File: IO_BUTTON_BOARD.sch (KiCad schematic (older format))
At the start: 118 parts

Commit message: Add reverse current protection, generate netlist, add footprints
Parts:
- added D2: D, Diodes_SMD:D_0805, symbol D
- C1: renamed from C?; footprint (none) -> Capacitors_SMD:c_elec_4x4.5
- D1, D10, D11, D12, D13, D14, D15, D16, D17, D18, D19, D3, D4, D5, D6, D7, D8, D9: renamed from D?; footprint (none) -> LEDs:LED_0805
- P1: renamed from P?; value I2C3 -> I2C; footprint (none) -> Pin_Headers:Pin_Header_Straight_1x04
- P10: renamed from P?; value IO_0 -> IO_7; footprint (none) -> Pin_Headers:Pin_Header_Straight_1x04
- P2, P3: renamed from P?; footprint (none) -> Pin_Headers:Pin_Header_Straight_1x04
- P4: renamed from P?; value IO_0 -> IO_1; footprint (none) -> Pin_Headers:Pin_Header_Straight_1x04
- P5: renamed from P?; value IO_0 -> IO_2; footprint (none) -> Pin_Headers:Pin_Header_Straight_1x04
- P6: renamed from P?; value IO_0 -> IO_3; footprint (none) -> Pin_Headers:Pin_Header_Straight_1x04
- P7: renamed from P?; value IO_0 -> IO_4; footprint (none) -> Pin_Headers:Pin_Header_Straight_1x04
- P8: renamed from P?; value IO_0 -> IO_5; footprint (none) -> Pin_Headers:Pin_Header_Straight_1x04
- P9: renamed from P?; value IO_0 -> IO_6; footprint (none) -> Pin_Headers:Pin_Header_Straight_1x04
- Q1, Q10, Q11, Q12, Q2, Q3, Q4, Q5, Q6, Q7, Q8, Q9: renamed from Q?; footprint (none) -> TO_SOT_Packages_SMD:SOT-23
- Q13: renamed from Q?; footprint (none) -> Resistors_SMD:R_0805
- R1, R10, R11, R12, R13, R14, R15, R16, R17, R18, R19, R2, R20, R21, R22, R23, R24, R25, R26, R27, R28, R29, R3, R30, R31, R32, R33, R34, R35, R36, R37, R38, R39, R4, R40, R41, R42, R43, R44, R45, R46, R47, R48, R49, R5, R50, R6, R7, R8, R9: renamed from R?; footprint (none) -> Resistors_SMD:R_0805
- S1, S2, S3, S4, S5, S6, S7, S8: renamed from S?; footprint (none) -> Pin_Headers:Pin_Header_Straight_1x03
- SW1: renamed from SW?; footprint (none) -> Housings_DIP:DIP-8_W7.62mm
- SW2, SW3, SW4, SW5, SW6, SW7, SW8, SW9: renamed from SW?; footprint (none) -> Buttons_Switches_SMD:SW_SPST_EVQPE1
- U1: renamed from U?; footprint (none) -> Housings_SOIC:SOIC-16W_7.5x10.3mm_Pitch1.27mm
- U2, U3: renamed from U?; footprint (none) -> SMD_Packages:SOIC-14_N
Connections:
- net +5V: now also D2.1 (K); no longer P1.3 (P3), P2.3 (P3)
- new net: D2.2 (A), P1.3 (P3), P2.3 (P3)
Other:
- moved on the sheet: C1, D3, P1, P2, R7

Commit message: Add pcb
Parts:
- Q13: footprint Resistors_SMD:R_0805 -> TO_SOT_Packages_SMD:SOT-23
- S1: value Switch2RT -> IN_0
- S2: value Switch2RT -> IN_1
- S3: value Switch2RT -> IN_2
- S4: value Switch2RT -> IN_3
- S5: value Switch2RT -> IN_4
- S6: value Switch2RT -> IN_5
- S7: value Switch2RT -> IN_6
- S8: value Switch2RT -> IN_7
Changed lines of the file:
@@
 F 0 "Q13" H 9700 10600 50  0000 L CNN
 F 1 "PNP" H 9700 10500 50  0000 L CNN
-F 2 "Resistors_SMD:R_0805" H 9700 10650 50  0001 C CNN
+F 2 "TO_SOT_Packages_SMD:SOT-23" H 9700 10650 50  0001 C CNN
 F 3 "" H 9500 10550 50  0000 C CNN
 	1    9500 10550
@@
 P 11000 700
 F 0 "S1" H 11000 450 60  0000 C CNN
-F 1 "Switch2RT" H 11000 950 60  0000 C CNN
+F 1 "IN_0" H 11000 950 60  0000 C CNN
 F 2 "Pin_Headers:Pin_Header_Straight_1x03" H 10700 750 60  0001 C CNN
 F 3 "" H 10700 750 60  0001 C CNN
@@
 P 11000 1150
 F 0 "S2" H 11000 900 60  0000 C CNN
-F 1 "Switch2RT" H 11000 1400 60  0000 C CNN
+F 1 "IN_1" H 11000 1400 60  0000 C CNN
 F 2 "Pin_Headers:Pin_Header_Straight_1x03" H 10700 1200 60  0001 C CNN
 F 3 "" H 10700 1200 60  0001 C CNN
@@
 P 11000 1600
 F 0 "S3" H 11000 1350 60  0000 C CNN
-F 1 "Switch2RT" H 11000 1850 60  0000 C CNN
+F 1 "IN_2" H 11000 1850 60  0000 C CNN
 F 2 "Pin_Headers:Pin_Header_Straight_1x03" H 10700 1650 60  0001 C CNN
 F 3 "" H 10700 1650 60  0001 C CNN
@@
 P 11000 2050
 F 0 "S4" H 11000 1800 60  0000 C CNN
-F 1 "Switch2RT" H 11000 2300 60  0000 C CNN
+F 1 "IN_3" H 11000 2300 60  0000 C CNN
 F 2 "Pin_Headers:Pin_Header_Straight_1x03" H 10700 2100 60  0001 C CNN
 F 3 "" H 10700 2100 60  0001 C CNN
@@
 P 11000 2650
 F 0 "S5" H 11000 2400 60  0000 C CNN
-F 1 "Switch2RT" H 11000 2900 60  0000 C CNN
+F 1 "IN_4" H 11000 2900 60  0000 C CNN
 F 2 "Pin_Headers:Pin_Header_Straight_1x03" H 10700 2700 60  0001 C CNN
 F 3 "" H 10700 2700 60  0001 C CNN
@@
 P 11000 3100
 F 0 "S6" H 11000 2850 60  0000 C CNN
-F 1 "Switch2RT" H 11000 3350 60  0000 C CNN
+F 1 "IN_5" H 11000 3350 60  0000 C CNN
 F 2 "Pin_Headers:Pin_Header_Straight_1x03" H 10700 3150 60  0001 C CNN
 F 3 "" H 10700 3150 60  0001 C CNN
@@
 P 11000 3550
 F 0 "S7" H 11000 3300 60  0000 C CNN
-F 1 "Switch2RT" H 11000 3800 60  0000 C CNN
+F 1 "IN_6" H 11000 3800 60  0000 C CNN
 F 2 "Pin_Headers:Pin_Header_Straight_1x03" H 10700 3600 60  0001 C CNN
 F 3 "" H 10700 3600 60  0001 C CNN
@@
 P 11000 4000
 F 0 "S8" H 11000 3750 60  0000 C CNN
-F 1 "Switch2RT" H 11000 4250 60  0000 C CNN
+F 1 "IN_7" H 11000 4250 60  0000 C CNN
 F 2 "Pin_Headers:Pin_Header_Straight_1x03" H 10700 4050 60  0001 C CNN
 F 3 "" H 10700 4050 60  0001 C CNN

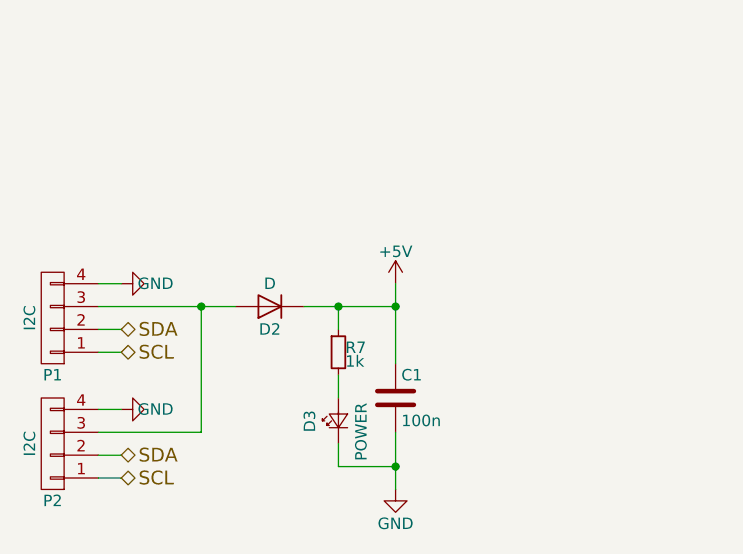
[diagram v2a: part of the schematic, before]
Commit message: Fix VCC disconnected issue Rerouted with larger width
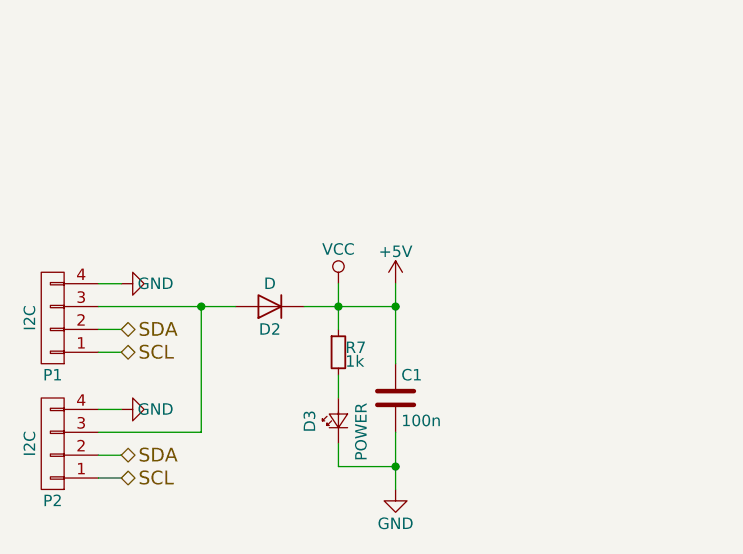
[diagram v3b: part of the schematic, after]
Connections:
- net VCC is gone; now on net +5V: U2.14 (VCC), U2.14 (VCC), U2.14 (VCC), U2.14 (VCC), U3.14 (VCC), U3.14 (VCC), U3.14 (VCC), U3.14 (VCC)
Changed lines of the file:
@@
 	1900 10600 1900 10500
 Wire Wire Line
-	1900 10300 1900 10200
+	1900 10100 1900 10300
 Wire Wire Line
 	1750 10200 2150 10200
@@
 Connection ~ 1900 10200
 Connection ~ 1300 10200
+$Comp
+L VCC #PWR?
+U 1 1 5C767C53
+P 1900 10100
+F 0 "#PWR?" H 1900 9950 50  0001 C CNN
+F 1 "VCC" H 1900 10250 50  0000 C CNN
+F 2 "" H 1900 10100 50  0000 C CNN
+F 3 "" H 1900 10100 50  0000 C CNN
+	1    1900 10100
+	1    0    0    -1
+$EndComp
 $EndSCHEMATC

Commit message: Reroute PCB with 'fake' +5V and GND netlist in order to get different width for PCB tracks
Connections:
- net +5V renamed VCC
- net OUT_0 renamed D_OUT_0
- net OUT_1 renamed D_OUT_1
- net OUT_2 renamed D_OUT_2
- net OUT_3 renamed D_OUT_3
- net OUT_4 renamed D_OUT_4
- net OUT_5 renamed D_OUT_5
- net OUT_6 renamed D_OUT_6
- net OUT_7 renamed D_OUT_7
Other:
- moved on the sheet: C1, D2, D3, P1, P2, R7

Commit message: Change positions and orientation of connectors on the pcb
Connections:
- net D_OUT_0: now also P3.3 (P3); no longer P3.2 (P2)
- net D_OUT_1: now also P4.3 (P3); no longer P4.2 (P2)
- net D_OUT_2: now also P5.3 (P3); no longer P5.2 (P2)
- net D_OUT_3: now also P6.3 (P3); no longer P6.2 (P2)
- net D_OUT_4: now also P7.3 (P3); no longer P7.2 (P2)
- net D_OUT_5: now also P8.3 (P3); no longer P8.2 (P2)
- net D_OUT_6: now also P9.3 (P3); no longer P9.2 (P2)
- net D_OUT_7: now also P10.3 (P3); no longer P10.2 (P2)
- net GND: now also P1.1 (P1), P10.1 (P1), P2.1 (P1), P3.1 (P1), P4.1 (P1), P5.1 (P1), P6.1 (P1), P7.1 (P1), P8.1 (P1), P9.1 (P1); no longer P1.4 (P4), P10.4 (P4), P2.4 (P4), P3.4 (P4), P4.4 (P4), P5.4 (P4), P6.4 (P4), P7.4 (P4), P8.4 (P4), P9.4 (P4)
- net IN_0: now also P3.2 (P2); no longer P3.3 (P3)
- net IN_1: now also P4.2 (P2); no longer P4.3 (P3)
- net IN_2: now also P5.2 (P2); no longer P5.3 (P3)
- net IN_3: now also P6.2 (P2); no longer P6.3 (P3)
- net IN_4: now also P7.2 (P2); no longer P7.3 (P3)
- net IN_5: now also P8.2 (P2); no longer P8.3 (P3)
- net IN_6: now also P9.2 (P2); no longer P9.3 (P3)
- net IN_7: now also P10.2 (P2); no longer P10.3 (P3)
- net SCL: now also P1.3 (P3), P2.3 (P3); no longer P1.1 (P1), P2.1 (P1)
- net SDA: now also P1.4 (P4), P2.4 (P4); no longer P1.2 (P2), P2.2 (P2)
- net VCC: now also P10.4 (P4), P3.4 (P4), P4.4 (P4), P5.4 (P4), P6.4 (P4), P7.4 (P4), P8.4 (P4), P9.4 (P4); no longer P10.1 (P1), P3.1 (P1), P4.1 (P1), P5.1 (P1), P6.1 (P1), P7.1 (P1), P8.1 (P1), P9.1 (P1)
- new net: D2.2 (A), P1.2 (P2), P2.2 (P2)
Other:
- moved on the sheet: P1, P2
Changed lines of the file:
@@
 L CONN_01X04 P2
 U 1 1 5C4ADA31
-P 650 9850
-F 0 "P2" H 650 10100 50  0000 C CNN
-F 1 "I2C" V 750 9850 50  0000 C CNN
-F 2 "Pin_Headers:Pin_Header_Straight_1x04" H 650 9850 50  0001 C CNN
-F 3 "" H 650 9850 50  0000 C CNN
-	1    650  9850
+P 650 9750
+F 0 "P2" H 650 10000 50  0000 C CNN
+F 1 "I2C" V 750 9750 50  0000 C CNN
+F 2 "Pin_Headers:Pin_Header_Straight_1x04" H 650 9750 50  0001 C CNN
+F 3 "" H 650 9750 50  0000 C CNN
+	1    650  9750
 	-1   0    0    1
 $EndComp
-Text HLabel 950  9900 2    60   BiDi ~ 0
+Text HLabel 950  9600 2    60   BiDi ~ 0
 SDA
-Text HLabel 950  10000 2    60   BiDi ~ 0
+Text HLabel 950  9700 2    60   BiDi ~ 0
 SCL
 Text HLabel 3700 4700 0    60   BiDi ~ 0
@@
 L CONN_01X04 P1
 U 1 1 5C4ADDFA
-P 650 9300
-F 0 "P1" H 650 9550 50  0000 C CNN
-F 1 "I2C" V 750 9300 50  0000 C CNN
-F 2 "Pin_Headers:Pin_Header_Straight_1x04" H 650 9300 50  0001 C CNN
-F 3 "" H 650 9300 50  0000 C CNN
-	1    650  9300
+P 650 9200
+F 0 "P1" H 650 9450 50  0000 C CNN
+F 1 "I2C" V 750 9200 50  0000 C CNN
+F 2 "Pin_Headers:Pin_Header_Straight_1x04" H 650 9200 50  0001 C CNN
+F 3 "" H 650 9200 50  0000 C CNN
+	1    650  9200
 	-1   0    0    1
 $EndComp
-Text HLabel 950  9350 2    60   BiDi ~ 0
+Text HLabel 950  9050 2    60   BiDi ~ 0
 SDA
-Text HLabel 950  9450 2    60   BiDi ~ 0
+Text HLabel 950  9150 2    60   BiDi ~ 0
 SCL
 $Comp
@@
 F 3 "" H 15900 900 50  0000 C CNN
 	1    15900 900
-	1    0    0    -1
+	1    0    0    1
 $EndComp
 $Comp
@@
 F 3 "" H 15900 1650 50  0000 C CNN
 	1    15900 1650
-	1    0    0    -1
+	1    0    0    1
 $EndComp
 $Comp
@@
 F 3 "" H 15900 2400 50  0000 C CNN
 	1    15900 2400
-	1    0    0    -1
+	1    0    0    1
 $EndComp
 $Comp
@@
 F 3 "" H 15900 3150 50  0000 C CNN
 	1    15900 3150
-	1    0    0    -1
+	1    0    0    1
 $EndComp
 $Comp
@@
 F 3 "" H 15900 3900 50  0000 C CNN
 	1    15900 3900
-	1    0    0    -1
+	1    0    0    1
 $EndComp
 $Comp
@@
 F 3 "" H 15900 4650 50  0000 C CNN
 	1    15900 4650
-	1    0    0    -1
+	1    0    0    1
 $EndComp
 $Comp
@@
 F 3 "" H 15900 5400 50  0000 C CNN
 	1    15900 5400
-	1    0    0    -1
+	1    0    0    1
 $EndComp
 $Comp
@@
 F 3 "" H 15900 6150 50  0000 C CNN
 	1    15900 6150
-	1    0    0    -1
+	1    0    0    1
 $EndComp
 $Comp
@@
 Connection ~ 2350 5100
 Wire Wire Line
+	850  9900 950  9900
+Wire Wire Line
+	1500 9800 850  9800
+Wire Wire Line
+	3700 4700 3800 4700
+Wire Wire Line
+	3800 4800 3700 4800
+Wire Wire Line
+	850  9600 950  9600
+Wire Wire Line
 	850  9700 950  9700
 Wire Wire Line
-	1500 9800 850  9800
-Wire Wire Line
-	3700 4700 3800 4700
-Wire Wire Line
-	3800 4800 3700 4800
-Wire Wire Line
-	850  9900 950  9900
-Wire Wire Line
-	850  10000 950  10000
+	850  9350 950  9350
+Wire Wire Line
+	850  9250 1650 9250
+Wire Wire Line
+	850  9050 950  9050
 Wire Wire Line
 	850  9150 950  9150
-Wire Wire Line
-	850  9250 1650 9250
-Wire Wire Line
-	850  9350 950  9350
-Wire Wire Line
-	850  9450 950  9450
 Wire Wire Line
 	2800 9650 2800 9550
@@
 Text HLabel 2050 10050 3    60   Input ~ 0
 GND_PWR
-Text HLabel 950  9700 2    60   Input ~ 0
+Text HLabel 950  9900 2    60   Input ~ 0
 GND_PWR
-Text HLabel 950  9150 2    60   Input ~ 0
+Text HLabel 950  9350 2    60   Input ~ 0
 GND_PWR
 Wire Wire Line

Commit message: Fix missing pull resistor Reroute PCB
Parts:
- added R51, R52, R53, R54, R55, R56, R57, R58: 1k, Resistors_SMD:R_0805, symbol R_Small
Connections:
- net IN_0: now also R51.1
- net IN_1: now also R52.1
- net IN_2: now also R53.1
- net IN_3: now also R54.1
- net IN_4: now also R55.1
- net IN_5: now also R56.1
- net IN_6: now also R57.1
- net IN_7: now also R58.1
- net PULL_LANE: now also R51.2, R52.2, R53.2, R54.2, R55.2, R56.2, R57.2, R58.2
- net D_OUT_0 renamed OUT_0
- net D_OUT_1 renamed OUT_1
- net D_OUT_2 renamed OUT_2
- net D_OUT_3 renamed OUT_3
- net D_OUT_4 renamed OUT_4
- net D_OUT_5 renamed OUT_5
- net D_OUT_6 renamed OUT_6
- net D_OUT_7 renamed OUT_7
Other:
- moved on the sheet: D3, R7

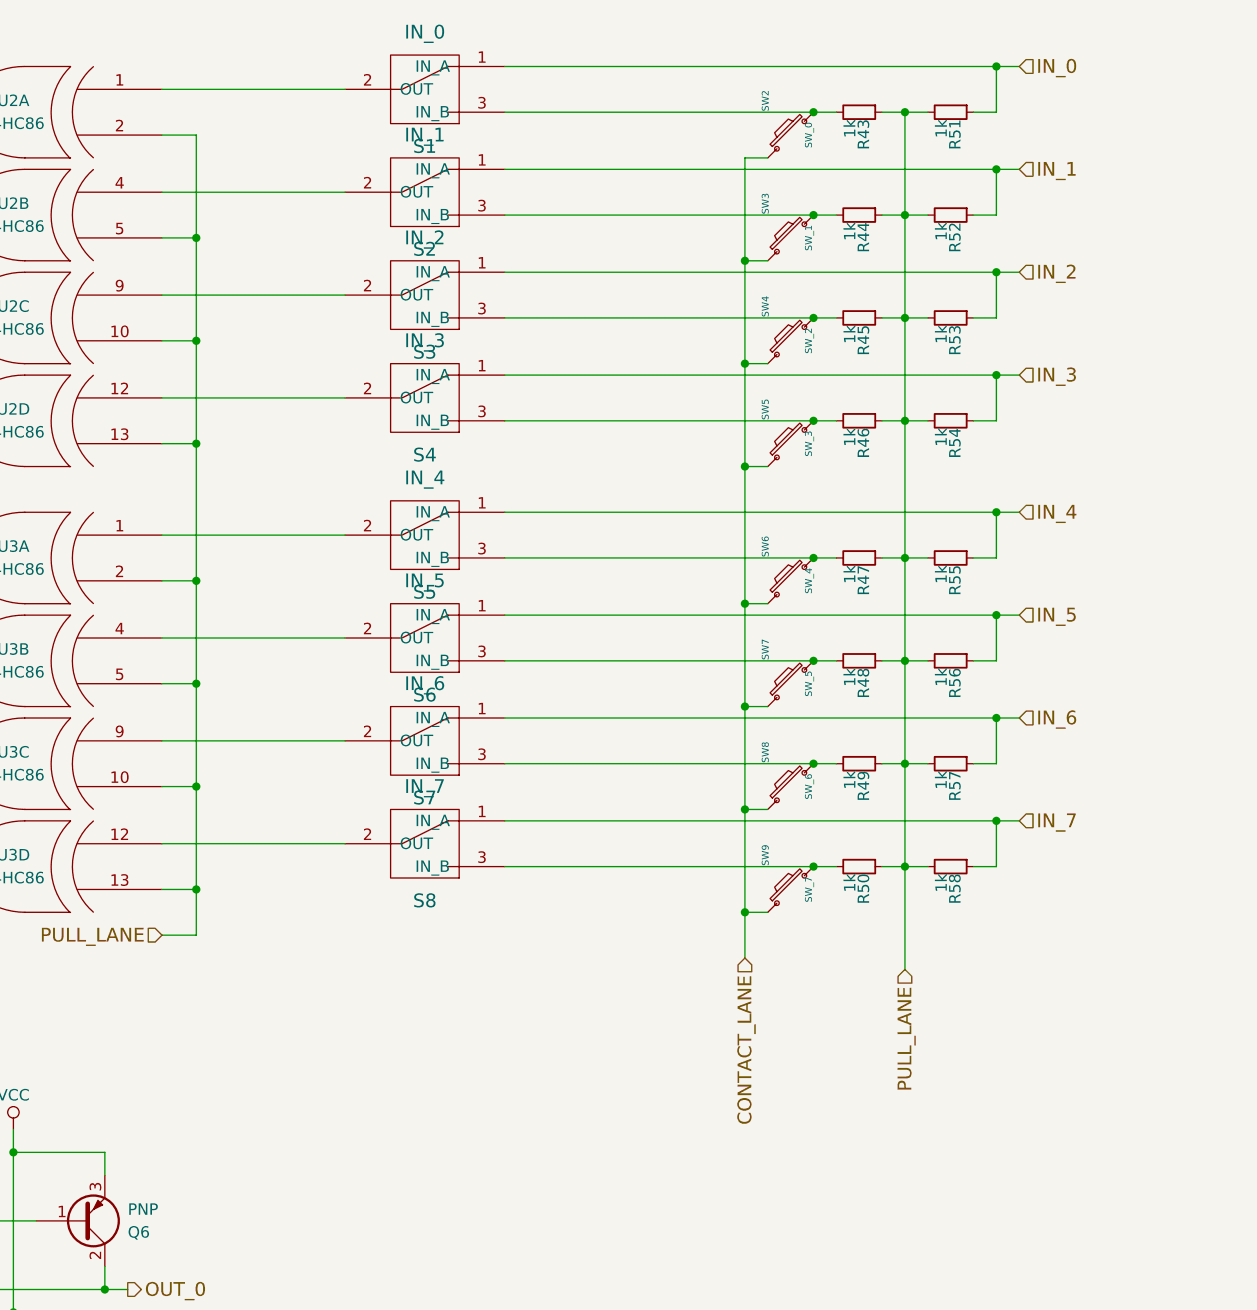
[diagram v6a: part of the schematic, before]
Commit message: Remove useless resistors Todo : develop a system to free XOR outputs on input mode
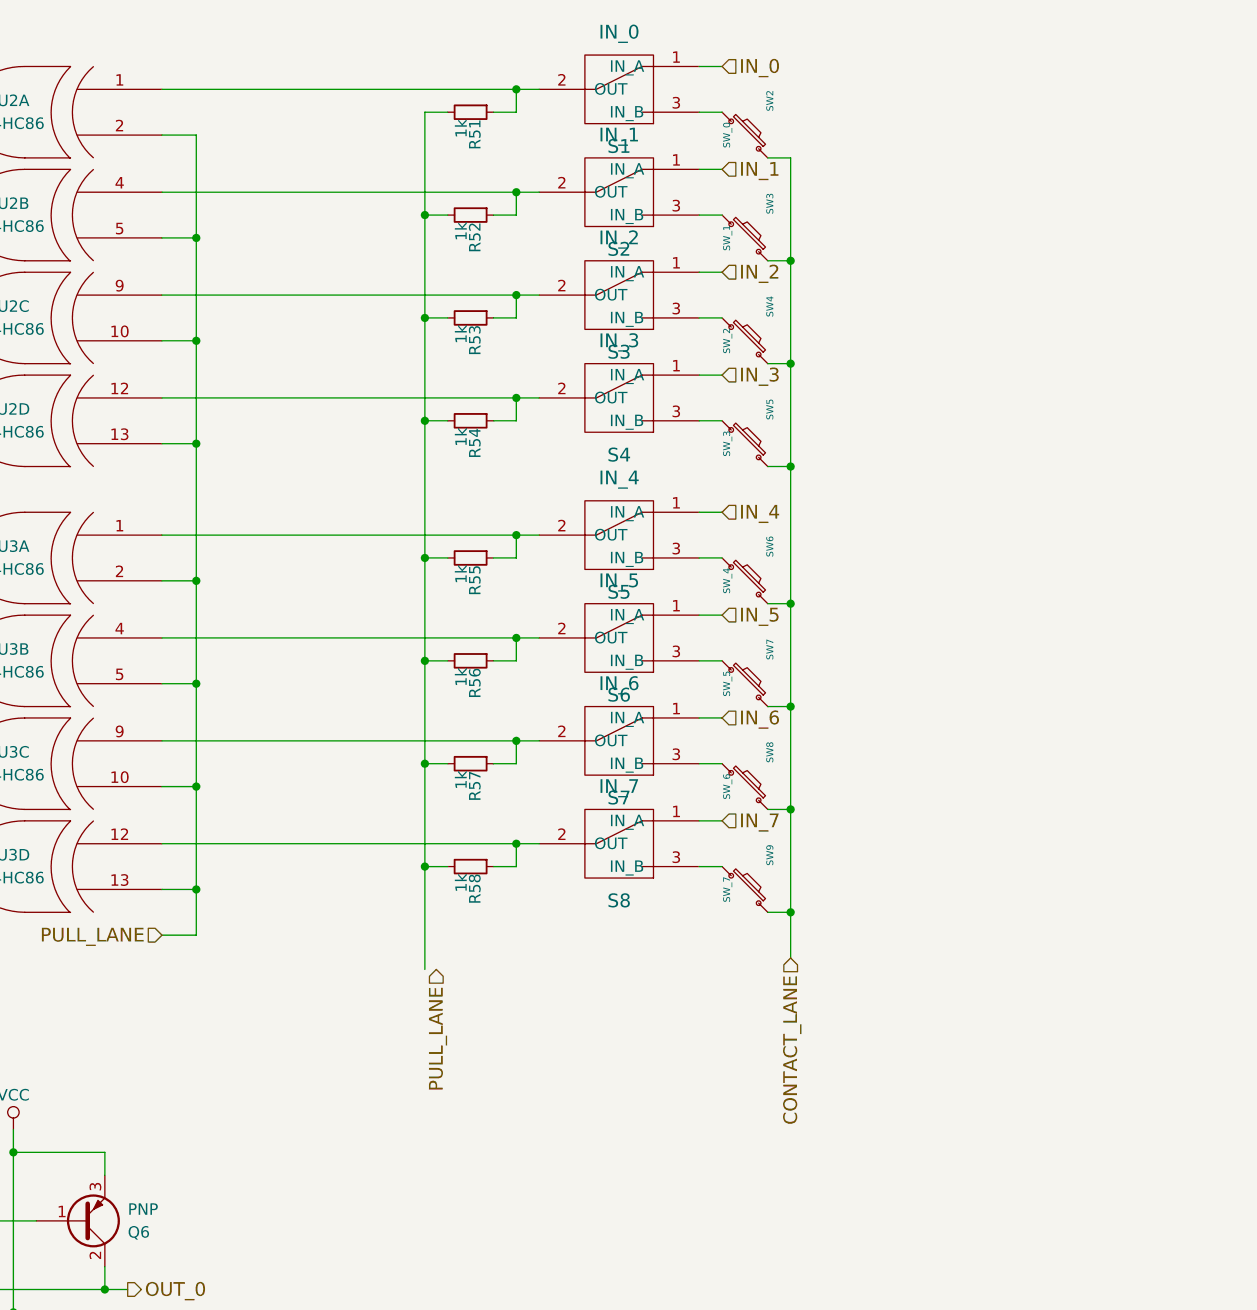
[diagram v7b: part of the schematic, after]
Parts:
- removed R43, R44, R45, R46, R47, R48, R49, R50: 1k, Resistors_SMD:R_0805, symbol R_Small
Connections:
- net IN_0: no longer R51.1
- net IN_1: no longer R52.1
- net IN_2: no longer R53.1
- net IN_3: no longer R54.1
- net IN_4: no longer R55.1
- net IN_5: no longer R56.1
- net IN_6: no longer R57.1
- net IN_7: no longer R58.1
- net PULL_LANE: no longer R51.2, R52.2, R53.2, R54.2, R55.2, R56.2, R57.2, R58.2
- net at S1.2 (OUT), U2.1 (IN1): now also R51.1
- net at S2.2 (OUT), U2.4 (IN1): now also R52.1
- net at S3.2 (OUT), U2.9 (IN1): now also R53.1
- net at S4.2 (OUT), U2.12 (IN1): now also R54.1
- net at S5.2 (OUT), U3.1 (IN1): now also R55.1
- net at S6.2 (OUT), U3.4 (IN1): now also R56.1
- net at S7.2 (OUT), U3.9 (IN1): now also R57.1
- net at S8.2 (OUT), U3.12 (IN1): now also R58.1
- new net: R51.2, R52.2, R53.2, R54.2, R55.2, R56.2, R57.2, R58.2
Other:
- moved on the sheet: R51, R52, R53, R54, R55, R56, R57, R58, S1, S2, S3, S4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
